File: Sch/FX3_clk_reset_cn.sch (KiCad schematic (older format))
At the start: 23 parts

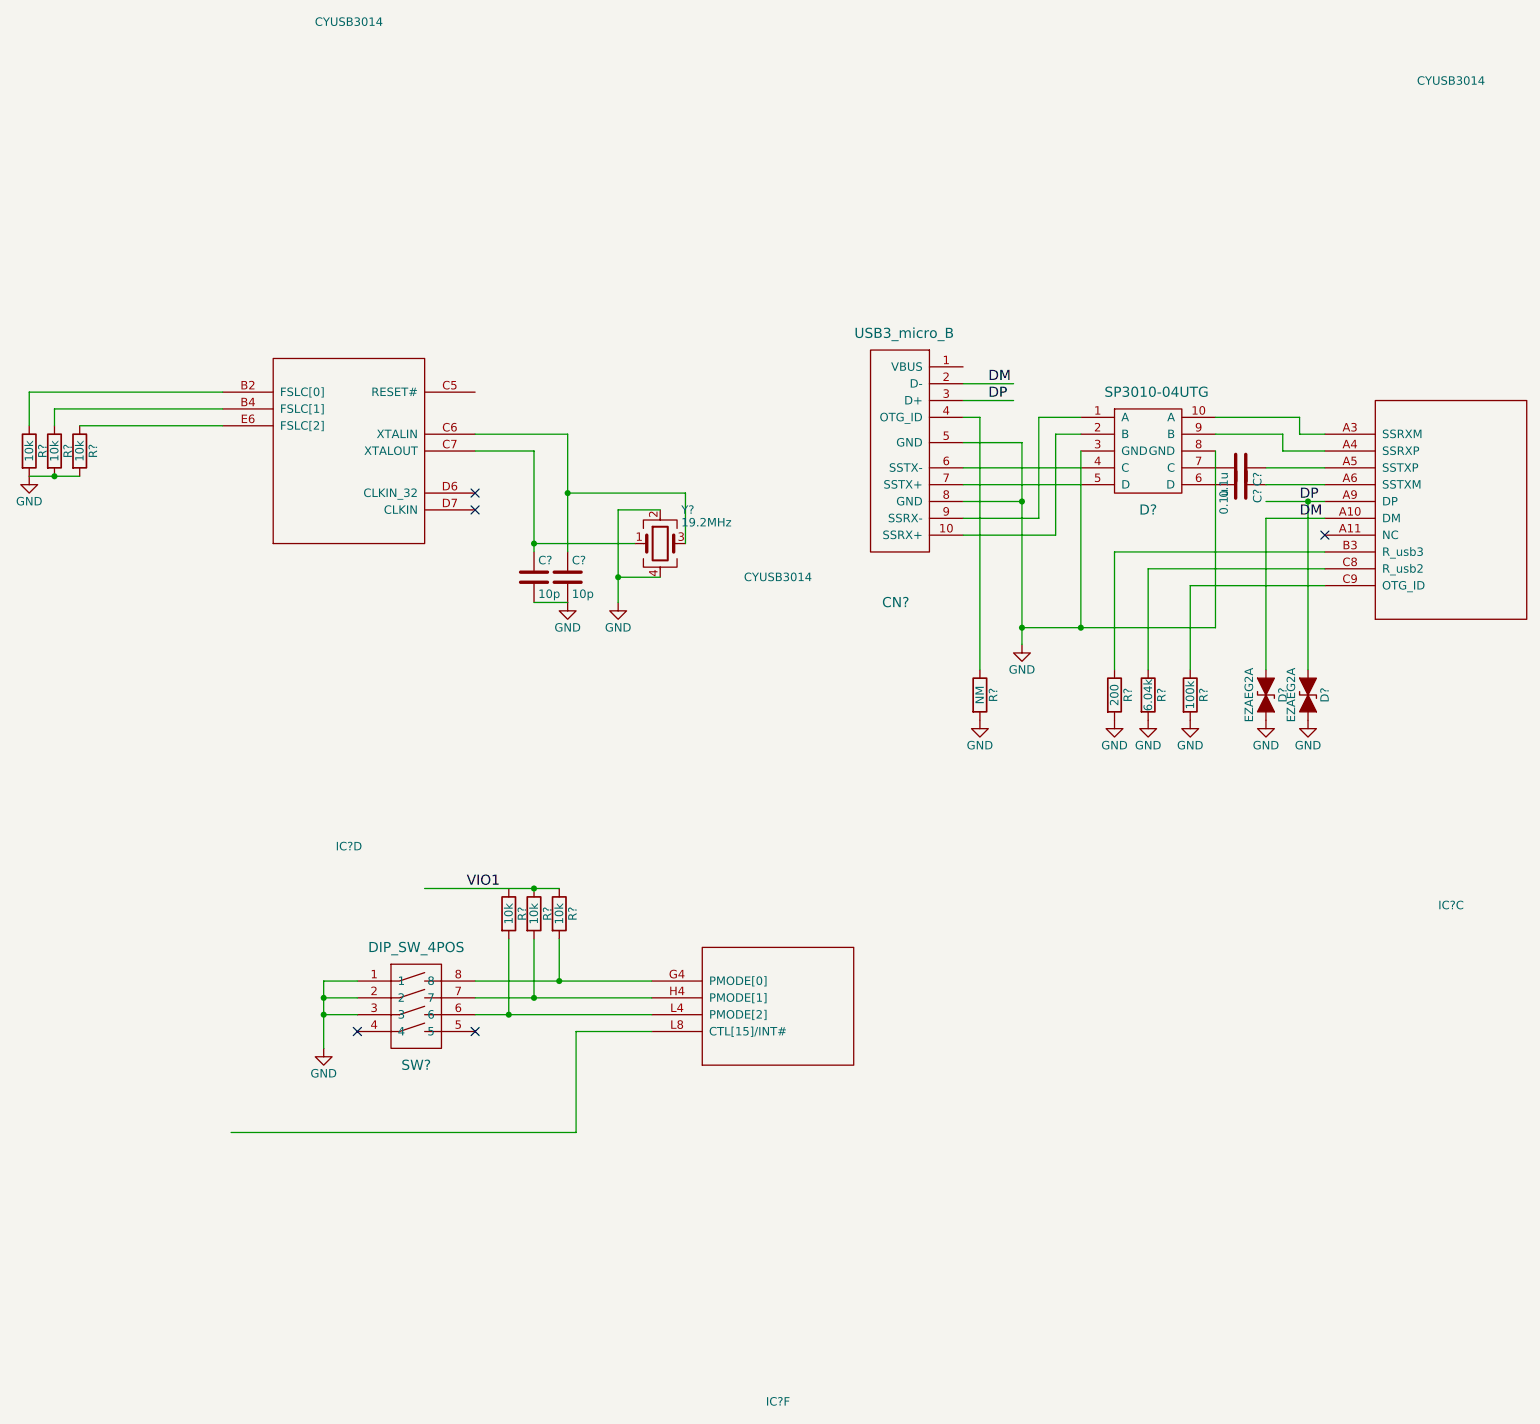
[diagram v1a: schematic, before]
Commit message: Add DQ and 80-pin
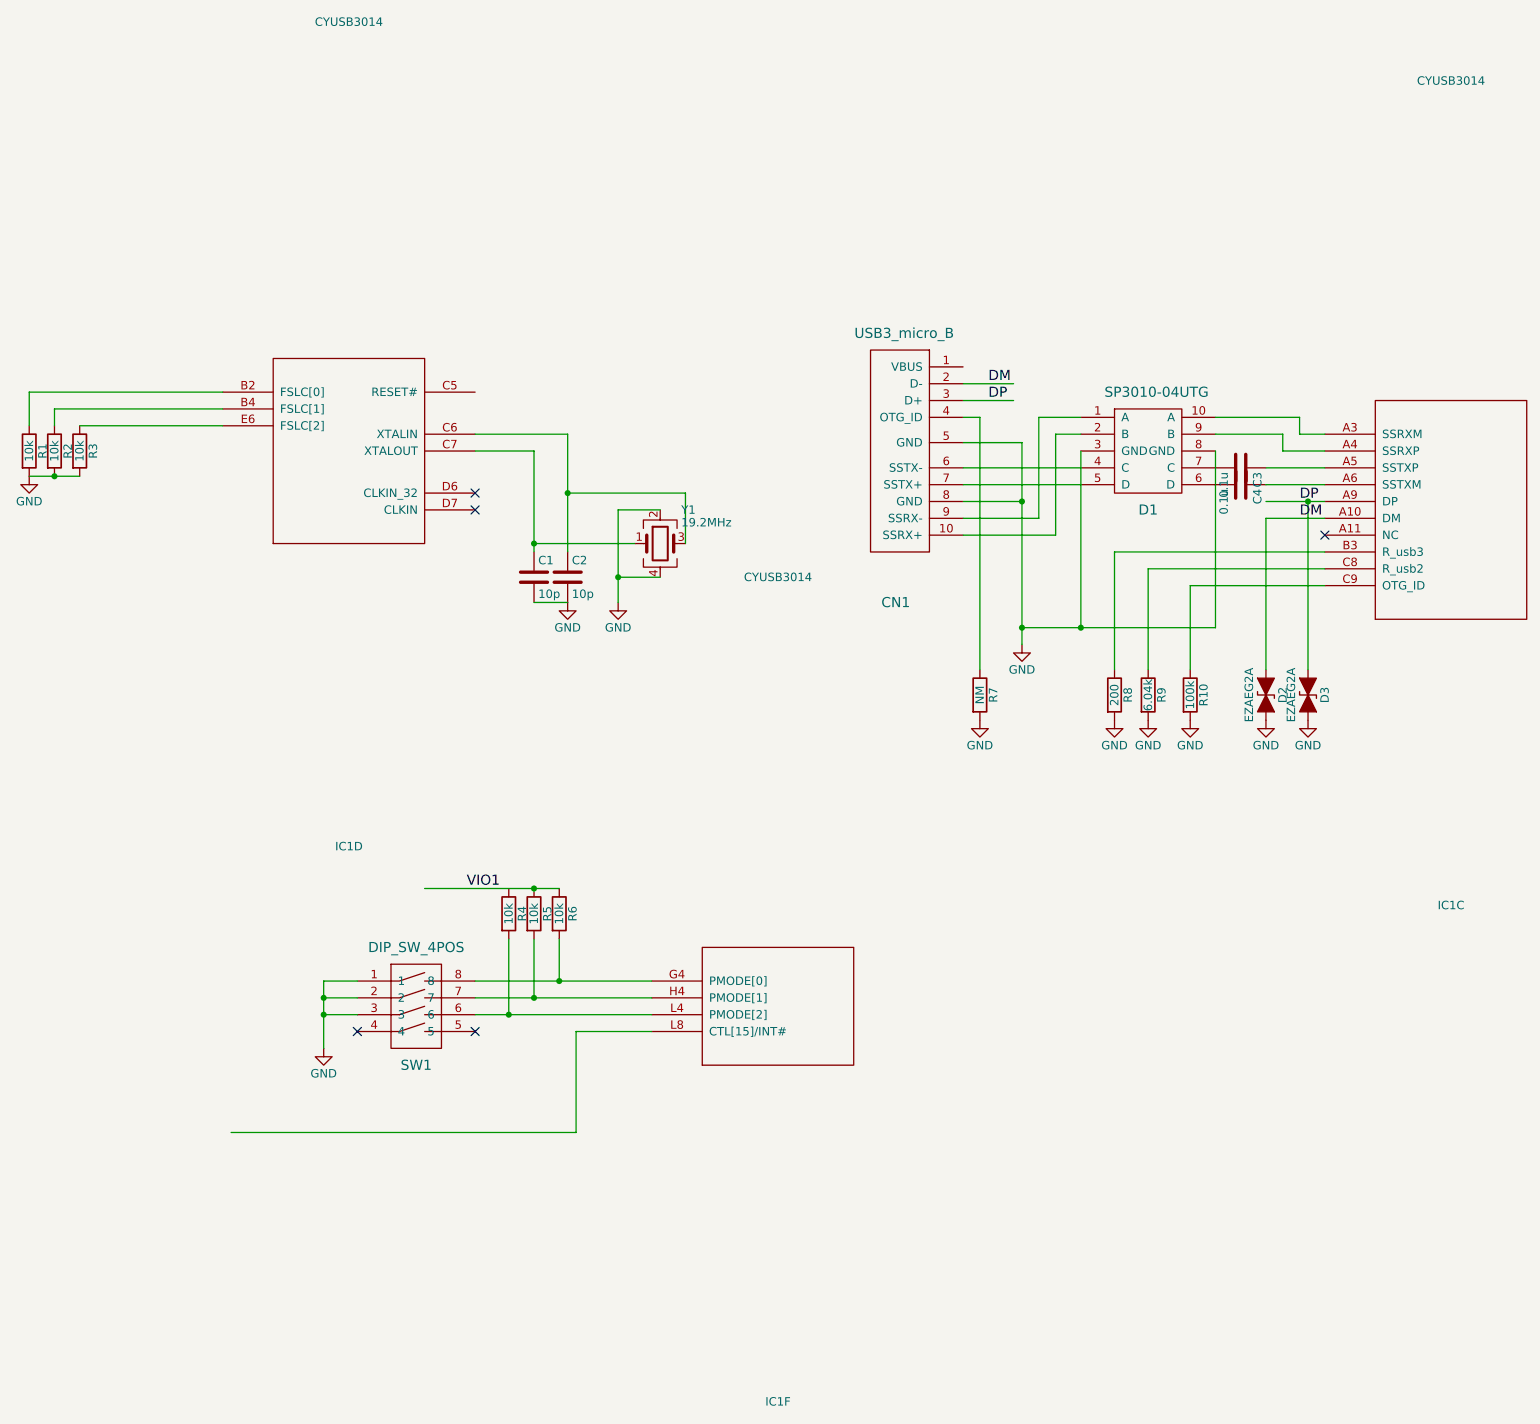
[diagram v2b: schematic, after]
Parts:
- gave numbers to parts that had none: 21
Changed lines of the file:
@@
 $Descr A4 11693 8268
 encoding utf-8
-Sheet 2 2
+Sheet 2 4
 Title ""
 Date ""
@@
 $EndDescr
 $Comp
-L GND #PWR?
+L GND #PWR4
 U 1 1 589AE25B
 P 4850 4200
-F 0 "#PWR?" H 4850 3950 50  0001 C CNN
+F 0 "#PWR4" H 4850 3950 50  0001 C CNN
 F 1 "GND" H 4850 4050 50  0000 C CNN
 F 2 "" H 4850 4200 50  0000 C CNN
@@
 $EndComp
 $Comp
-L Crystal_GND24 Y?
+L Crystal_GND24 Y1
 U 1 1 589AE261
 P 5100 3850
-F 0 "Y?" H 5225 4050 50  0000 L CNN
+F 0 "Y1" H 5225 4050 50  0000 L CNN
 F 1 "19.2MHz" H 5225 3975 50  0000 L CNN
 F 2 "" H 5100 3850 50  0000 C CNN
@@
 $EndComp
 $Comp
-L GND #PWR?
+L GND #PWR3
 U 1 1 589AE268
 P 4550 4200
-F 0 "#PWR?" H 4550 3950 50  0001 C CNN
+F 0 "#PWR3" H 4550 3950 50  0001 C CNN
 F 1 "GND" H 4550 4050 50  0000 C CNN
 F 2 "" H 4550 4200 50  0000 C CNN
@@
 $EndComp
 $Comp
-L C C?
+L C C1
 U 1 1 589AE26E
 P 4350 4050
-F 0 "C?" H 4375 4150 50  0000 L CNN
+F 0 "C1" H 4375 4150 50  0000 L CNN
 F 1 "10p" H 4375 3950 50  0000 L CNN
 F 2 "" H 4388 3900 50  0000 C CNN
@@
 $EndComp
 $Comp
-L C C?
+L C C2
 U 1 1 589AE275
 P 4550 4050
-F 0 "C?" H 4575 4150 50  0000 L CNN
+F 0 "C2" H 4575 4150 50  0000 L CNN
 F 1 "10p" H 4575 3950 50  0000 L CNN
 F 2 "" H 4588 3900 50  0000 C CNN
@@
 $EndComp
 $Comp
-L GND #PWR?
+L GND #PWR1
 U 1 1 589AE27C
 P 1350 3450
-F 0 "#PWR?" H 1350 3200 50  0001 C CNN
+F 0 "#PWR1" H 1350 3200 50  0001 C CNN
 F 1 "GND" H 1350 3300 50  0000 C CNN
 F 2 "" H 1350 3450 50  0000 C CNN
@@
 $EndComp
 $Comp
-L R R?
+L R R1
 U 1 1 589AE282
 P 1350 3300
-F 0 "R?" V 1430 3300 50  0000 C CNN
+F 0 "R1" V 1430 3300 50  0000 C CNN
 F 1 "10k" V 1350 3300 50  0000 C CNN
 F 2 "" V 1280 3300 50  0000 C CNN
@@
 $EndComp
 $Comp
-L R R?
+L R R2
 U 1 1 589AE289
 P 1500 3300
-F 0 "R?" V 1580 3300 50  0000 C CNN
+F 0 "R2" V 1580 3300 50  0000 C CNN
 F 1 "10k" V 1500 3300 50  0000 C CNN
 F 2 "" V 1430 3300 50  0000 C CNN
@@
 $EndComp
 $Comp
-L R R?
+L R R3
 U 1 1 589AE290
 P 1650 3300
-F 0 "R?" V 1730 3300 50  0000 C CNN
+F 0 "R3" V 1730 3300 50  0000 C CNN
 F 1 "10k" V 1650 3300 50  0000 C CNN
 F 2 "" V 1580 3300 50  0000 C CNN
@@
 $EndComp
 $Comp
-L USB3_micro_B CN?
+L USB3_micro_B CN1
 U 1 1 589AE710
 P 6500 3350
-F 0 "CN?" H 6500 2500 60  0000 C CNN
+F 0 "CN1" H 6500 2500 60  0000 C CNN
 F 1 "USB3_micro_B" H 6550 4100 60  0000 C CNN
 F 2 "" H 6500 2500 60  0001 C CNN
@@
 $EndComp
 $Comp
-L C C?
+L C C3
 U 1 1 589AE887
 P 8550 3400
-F 0 "C?" H 8575 3500 50  0000 L CNN
+F 0 "C3" H 8575 3500 50  0000 L CNN
 F 1 "0.1u" H 8575 3300 50  0000 L CNN
 F 2 "" H 8588 3250 50  0000 C CNN
@@
 $EndComp
 $Comp
-L C C?
+L C C4
 U 1 1 589AE915
 P 8550 3500
-F 0 "C?" H 8575 3600 50  0000 L CNN
+F 0 "C4" H 8575 3600 50  0000 L CNN
 F 1 "0.1u" H 8575 3400 50  0000 L CNN
 F 2 "" H 8588 3350 50  0000 C CNN
@@
 $EndComp
 $Comp
-L SP3010-04UTG D?
+L SP3010-04UTG D1
 U 1 1 589AEAF9
 P 8000 3300
-F 0 "D?" H 8000 2950 60  0000 C CNN
+F 0 "D1" H 8000 2950 60  0000 C CNN
 F 1 "SP3010-04UTG" H 8050 3650 60  0000 C CNN
 F 2 "" H 8000 2950 60  0001 C CNN
@@
 $EndComp
 $Comp
-L GND #PWR?
+L GND #PWR6
 U 1 1 589AEE63
 P 7250 4450
-F 0 "#PWR?" H 7250 4200 50  0001 C CNN
+F 0 "#PWR6" H 7250 4200 50  0001 C CNN
 F 1 "GND" H 7250 4300 50  0000 C CNN
 F 2 "" H 7250 4450 50  0000 C CNN
@@
 $EndComp
 $Comp
-L CYUSB3014 IC?
+L CYUSB3014 IC1
 U 3 1 58A04A1C
 P 9800 3650
-F 0 "IC?" H 9800 1300 50  0000 C CNN
+F 0 "IC1" H 9800 1300 50  0000 C CNN
 F 1 "CYUSB3014" H 9800 6200 50  0000 C CNN
 F 2 "MODULE" H 9750 5950 50  0001 C CNN
@@
 $EndComp
 $Comp
-L CYUSB3014 IC?
+L CYUSB3014 IC1
 U 4 1 58A04C42
 P 3250 3300
-F 0 "IC?" H 3250 950 50  0000 C CNN
+F 0 "IC1" H 3250 950 50  0000 C CNN
 F 1 "CYUSB3014" H 3250 5850 50  0000 C CNN
 F 2 "MODULE" H 3200 5600 50  0001 C CNN
@@
 NoConn ~ 4000 3650
 $Comp
-L D_TVS_ALT D?
+L D_TVS_ALT D2
 U 1 1 58A0529E
 P 8700 4750
-F 0 "D?" H 8700 4850 50  0000 C CNN
+F 0 "D2" H 8700 4850 50  0000 C CNN
 F 1 "EZAEG2A" H 8700 4650 50  0000 C CNN
 F 2 "" H 8700 4750 50  0000 C CNN
@@
 $EndComp
 $Comp
-L D_TVS_ALT D?
+L D_TVS_ALT D3
 U 1 1 58A0531B
 P 8950 4750
-F 0 "D?" H 8950 4850 50  0000 C CNN
+F 0 "D3" H 8950 4850 50  0000 C CNN
 F 1 "EZAEG2A" H 8950 4650 50  0000 C CNN
 F 2 "" H 8950 4750 50  0000 C CNN
@@
 $EndComp
 $Comp
-L GND #PWR?
+L GND #PWR10
 U 1 1 58A053A3
 P 8700 4900
-F 0 "#PWR?" H 8700 4650 50  0001 C CNN
+F 0 "#PWR10" H 8700 4650 50  0001 C CNN
 F 1 "GND" H 8700 4750 50  0000 C CNN
 F 2 "" H 8700 4900 50  0000 C CNN
@@
 $EndComp
 $Comp
-L GND #PWR?
+L GND #PWR11
 U 1 1 58A0545F
 P 8950 4900
-F 0 "#PWR?" H 8950 4650 50  0001 C CNN
+F 0 "#PWR11" H 8950 4650 50  0001 C CNN
 F 1 "GND" H 8950 4750 50  0000 C CNN
 F 2 "" H 8950 4900 50  0000 C CNN
@@
 NoConn ~ 9050 3800
 $Comp
-L R R?
+L R R8
 U 1 1 58A05CC7
 P 7800 4750
-F 0 "R?" V 7880 4750 50  0000 C CNN
+F 0 "R8" V 7880 4750 50  0000 C CNN
 F 1 "200" V 7800 4750 50  0000 C CNN
 F 2 "" V 7730 4750 50  0000 C CNN
@@
 $EndComp
 $Comp
-L R R?
+L R R9
 U 1 1 58A05D73
 P 8000 4750
-F 0 "R?" V 8080 4750 50  0000 C CNN
+F 0 "R9" V 8080 4750 50  0000 C CNN
 F 1 "6.04k" V 8000 4750 50  0000 C CNN
 F 2 "" V 7930 4750 50  0000 C CNN
@@
 $EndComp
 $Comp
-L GND #PWR?
+L GND #PWR7
 U 1 1 58A05EBD
 P 7800 4900
-F 0 "#PWR?" H 7800 4650 50  0001 C CNN
+F 0 "#PWR7" H 7800 4650 50  0001 C CNN
 F 1 "GND" H 7800 4750 50  0000 C CNN
 F 2 "" H 7800 4900 50  0000 C CNN
@@
 $EndComp
 $Comp
-L GND #PWR?
+L GND #PWR8
 U 1 1 58A05EE5
 P 8000 4900
-F 0 "#PWR?" H 8000 4650 50  0001 C CNN
+F 0 "#PWR8" H 8000 4650 50  0001 C CNN
 F 1 "GND" H 8000 4750 50  0000 C CNN
 F 2 "" H 8000 4900 50  0000 C CNN
@@
 $EndComp
 $Comp
-L R R?
+L R R10
 U 1 1 58A06131
 P 8250 4750
-F 0 "R?" V 8330 4750 50  0000 C CNN
+F 0 "R10" V 8330 4750 50  0000 C CNN
 F 1 "100k" V 8250 4750 50  0000 C CNN
 F 2 "" V 8180 4750 50  0000 C CNN
@@
 $EndComp
 $Comp
-L GND #PWR?
+L GND #PWR9
 U 1 1 58A06182
 P 8250 4900
-F 0 "#PWR?" H 8250 4650 50  0001 C CNN
+F 0 "#PWR9" H 8250 4650 50  0001 C CNN
 F 1 "GND" H 8250 4750 50  0000 C CNN
 F 2 "" H 8250 4900 50  0000 C CNN
@@
 $EndComp
 $Comp
-L R R?
+L R R7
 U 1 1 58A0634C
 P 7000 4750
-F 0 "R?" V 7080 4750 50  0000 C CNN
+F 0 "R7" V 7080 4750 50  0000 C CNN
 F 1 "NM" V 7000 4750 50  0000 C CNN
 F 2 "" V 6930 4750 50  0000 C CNN
@@
 $EndComp
 $Comp
-L GND #PWR?
+L GND #PWR5
 U 1 1 58A06620
 P 7000 4900
-F 0 "#PWR?" H 7000 4650 50  0001 C CNN
+F 0 "#PWR5" H 7000 4650 50  0001 C CNN
 F 1 "GND" H 7000 4750 50  0000 C CNN
 F 2 "" H 7000 4900 50  0000 C CNN
@@
 $EndComp
 $Comp
-L CYUSB3014 IC?
+L CYUSB3014 IC1
 U 6 1 58A06F9C
 P 5800 6600
-F 0 "IC?" H 5800 4250 50  0000 C CNN
+F 0 "IC1" H 5800 4250 50  0000 C CNN
 F 1 "CYUSB3014" H 5800 9150 50  0000 C CNN
 F 2 "MODULE" H 5750 8900 50  0001 C CNN
@@
 VIO1
 $Comp
-L R R?
+L R R4
 U 1 1 58A073A6
 P 4200 6050
-F 0 "R?" V 4280 6050 50  0000 C CNN
+F 0 "R4" V 4280 6050 50  0000 C CNN
 F 1 "10k" V 4200 6050 50  0000 C CNN
 F 2 "" V 4130 6050 50  0000 C CNN
@@
 $EndComp
 $Comp
-L R R?
+L R R5
 U 1 1 58A07409
 P 4350 6050
-F 0 "R?" V 4430 6050 50  0000 C CNN
+F 0 "R5" V 4430 6050 50  0000 C CNN
 F 1 "10k" V 4350 6050 50  0000 C CNN
 F 2 "" V 4280 6050 50  0000 C CNN
@@
 $EndComp
 $Comp
-L R R?
+L R R6
 U 1 1 58A07452
 P 4500 6050
-F 0 "R?" V 4580 6050 50  0000 C CNN
+F 0 "R6" V 4580 6050 50  0000 C CNN
 F 1 "10k" V 4500 6050 50  0000 C CNN
 F 2 "" V 4430 6050 50  0000 C CNN
@@
 	4000 6650 5050 6650
 $Comp
-L GND #PWR?
+L GND #PWR2
 U 1 1 58A077E4
 P 3100 6850
-F 0 "#PWR?" H 3100 6600 50  0001 C CNN
+F 0 "#PWR2" H 3100 6600 50  0001 C CNN
 F 1 "GND" H 3100 6700 50  0000 C CNN
 F 2 "" H 3100 6850 50  0000 C CNN
@@
 $EndComp
 $Comp
-L DIP_SW_4POS SW?
+L DIP_SW_4POS SW1
 U 1 1 58A07985
 P 3650 6600
-F 0 "SW?" H 3650 6250 60  0000 C CNN
+F 0 "SW1" H 3650 6250 60  0000 C CNN
 F 1 "DIP_SW_4POS" H 3650 6950 60  0000 C CNN
 F 2 "" H 3750 6450 60  0001 C CNN
